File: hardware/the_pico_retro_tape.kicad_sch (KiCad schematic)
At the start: 13 parts, among them J1 SD Card Modul, J2 Conn_01x06, J3 TFT Display ST7735, Q1 BC547, SW1 UP BUTTON, SW2 DOWN BUTTON, SW3 ENTER BUTTON, SW4 PLAY BUTTON, U1 Pico

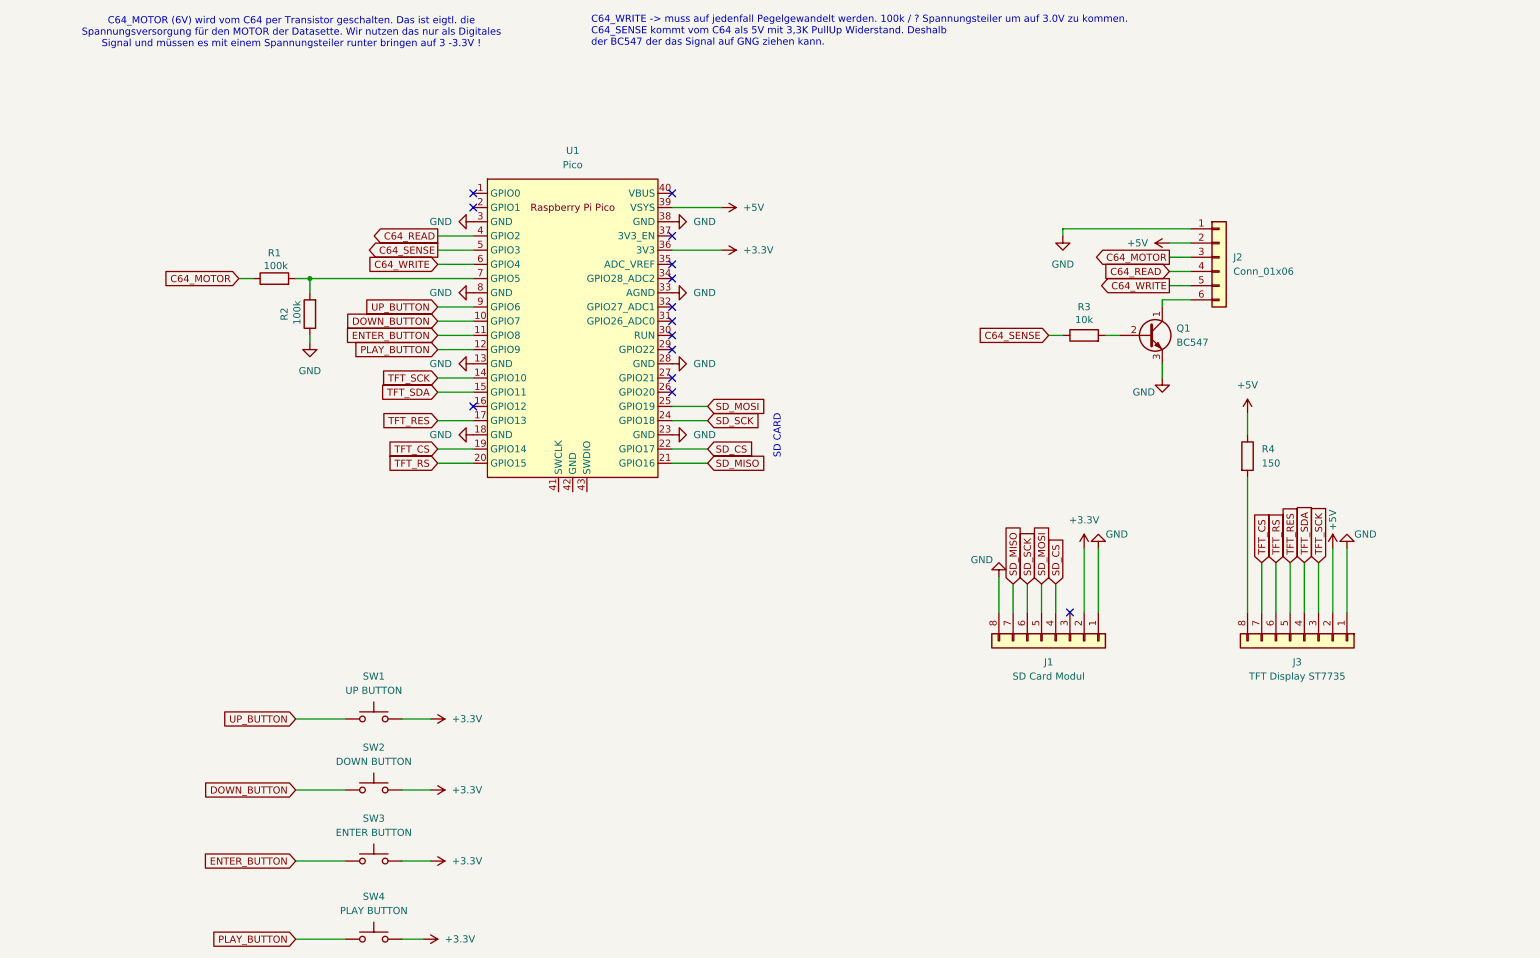
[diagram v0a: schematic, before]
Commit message: hardware:  added an optional speaker
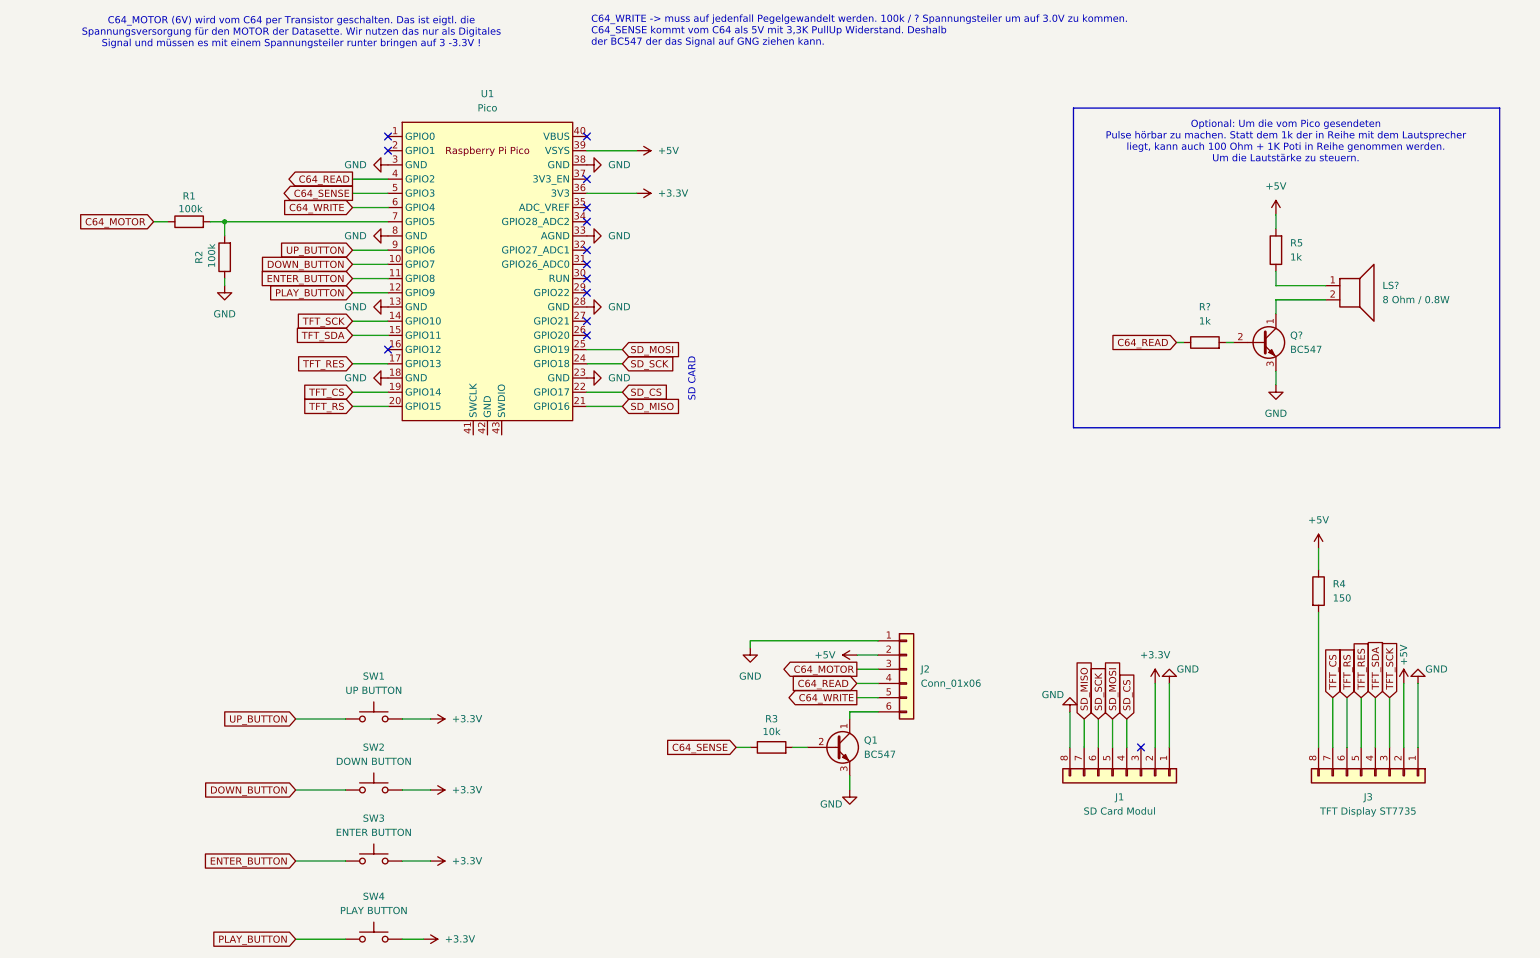
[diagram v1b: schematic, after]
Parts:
- added LS?: 8 Ohm / 0.8W, symbol Device:Speaker
- added Q?: BC547, Package_TO_SOT_THT:TO-92_Inline, symbol Transistor_BJT:BC547
- added R5, R?: 1k, symbol Device:R
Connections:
- net +5V: now also R5.2
- net C64_READ: now also R?.1
- net GND: now also Q?.3 (E)
- new net: LS?.1, R5.1
- new net: LS?.2, Q?.1 (C)
- new net: Q?.2 (B), R?.2
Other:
- note added: "Optional: Um die vom Pico gesendeten Pulse hörbar zu machen. Statt dem 1k der in Reihe mit dem Lautsprecher liegt, kann auch 100 Ohm + 1K Poti in Reihe genommen werden. Um die Lautstärke zu steuern."
- moved on the sheet: J1, J2, J3, Q1, R1, R2, R3, R4, U1

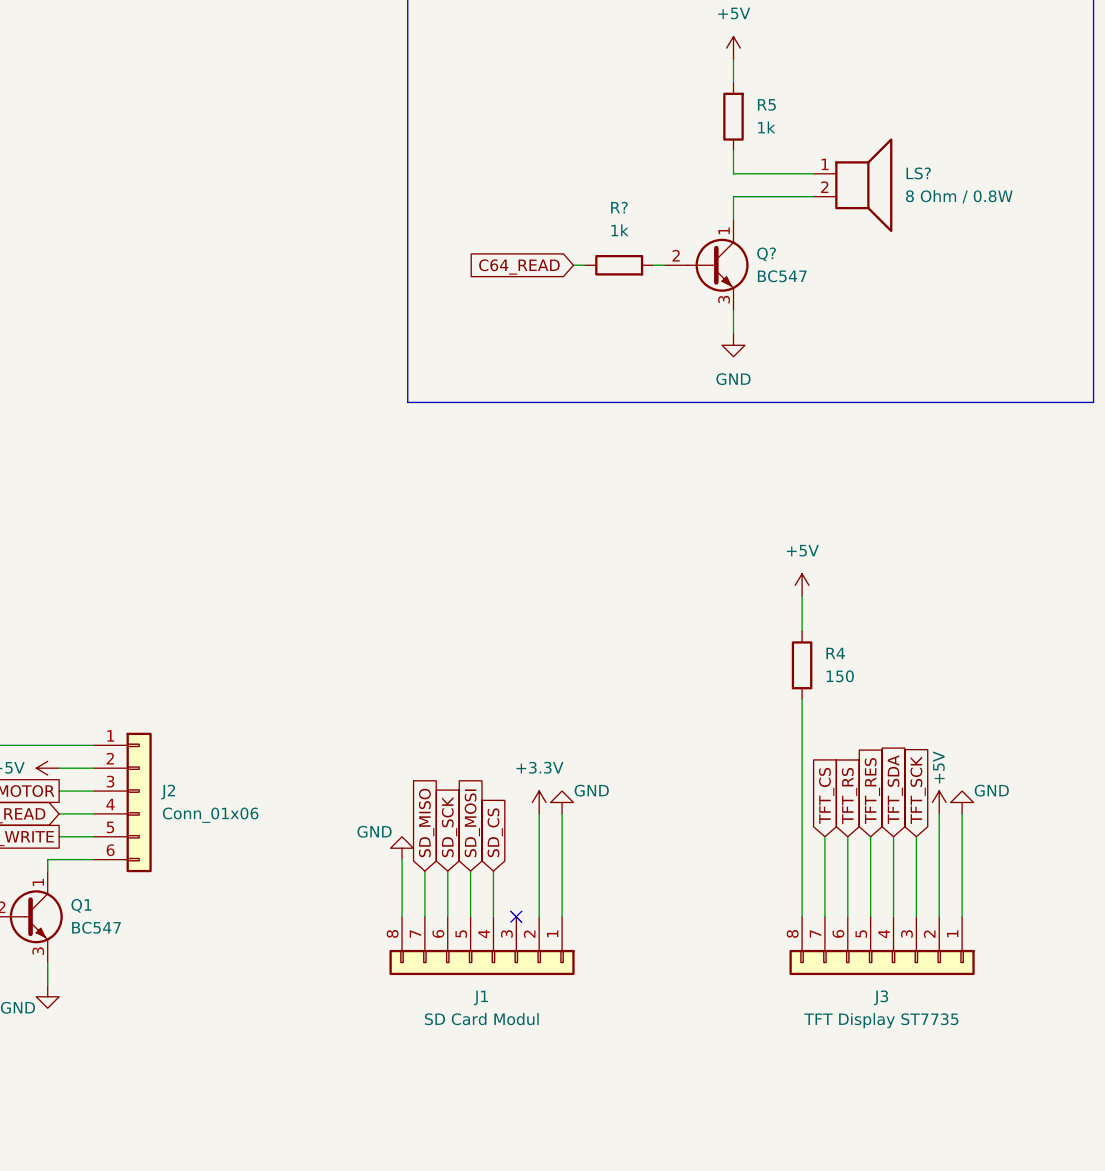
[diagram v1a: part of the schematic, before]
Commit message: Update schematic references and correct plot directory path
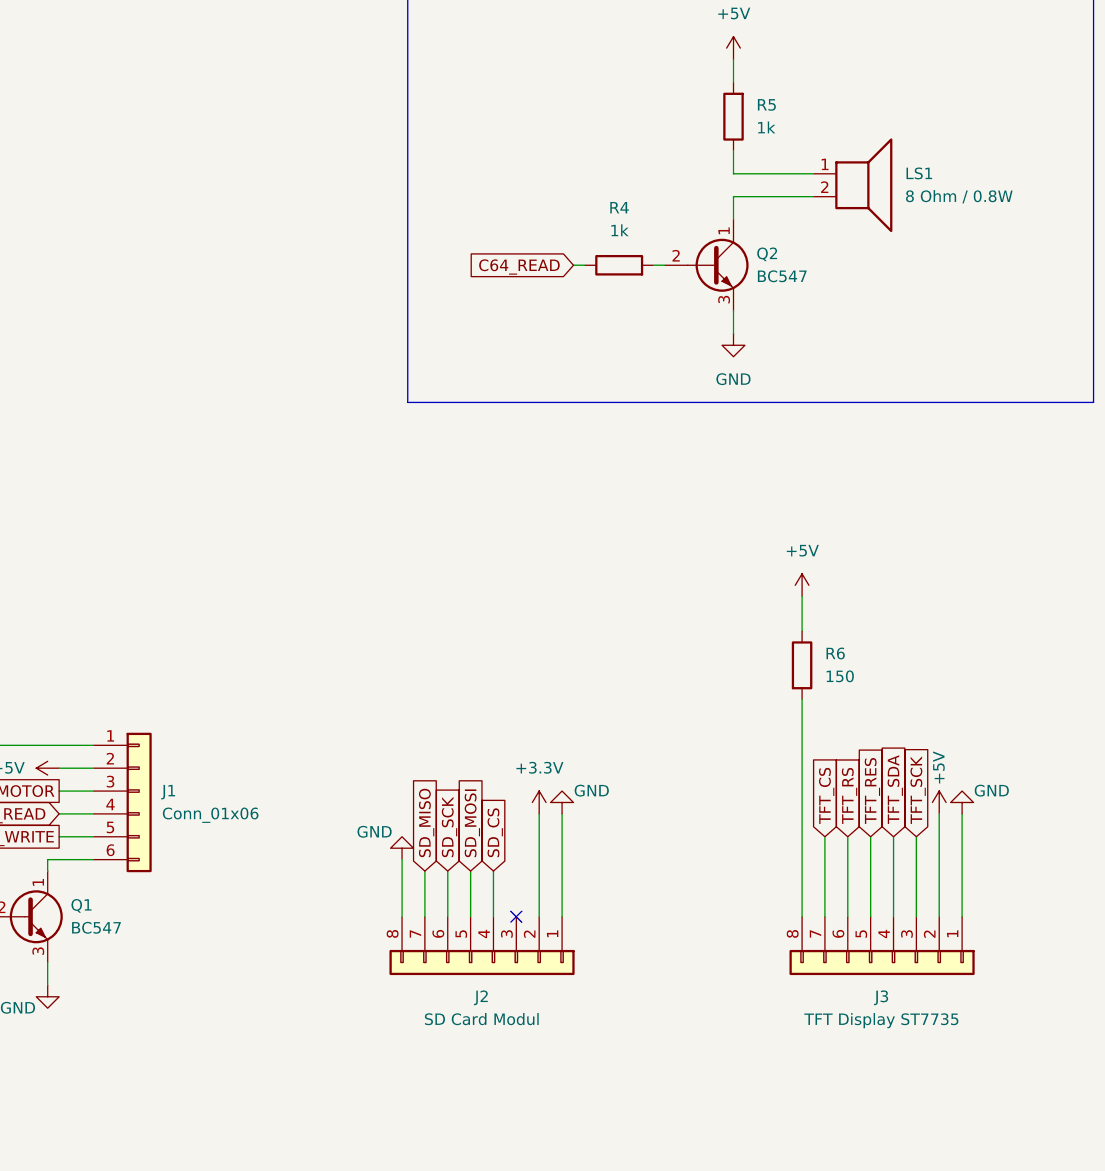
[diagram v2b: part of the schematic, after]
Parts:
- gave numbers to parts that had none: 3
- renumbered J2 to J1, J1 to J2, R4 to R6
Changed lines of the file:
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@@
 		(dnp no)
 		(fields_autoplaced yes)
-		(property "Reference" "#PWR03"
+		(property "Reference" "#PWR07"
 			(at 77.47 142.24 0)
 			(effects
@@
 			(project "the_pico_retro_tape"
 				(path "/58eb91ea-7f3f-48ec-bf75-2e4d8bc1bbc2"
-					(reference "#PWR03")
+					(reference "#PWR07")
 					(unit 1)
 				)
@@
 		(dnp no)
 		(fields_autoplaced yes)
-		(property "Reference" "#PWR04"
+		(property "Reference" "#PWR08"
 			(at 77.47 154.94 0)
 			(effects
@@
 			(project "the_pico_retro_tape"
 				(path "/58eb91ea-7f3f-48ec-bf75-2e4d8bc1bbc2"
-					(reference "#PWR04")
+					(reference "#PWR08")
 					(unit 1)
 				)
@@
 		(dnp no)
 		(fields_autoplaced yes)
-		(property "Reference" "#PWR018"
+		(property "Reference" "#PWR020"
 			(at 210.82 139.7 0)
 			(effects
@@
 			(project "the_pico_retro_tape"
 				(path "/58eb91ea-7f3f-48ec-bf75-2e4d8bc1bbc2"
-					(reference "#PWR018")
+					(reference "#PWR020")
 					(unit 1)
 				)
@@
 		(dnp no)
 		(fields_autoplaced yes)
-		(property "Reference" "#PWR021"
+		(property "Reference" "#PWR018"
 			(at 161.29 130.81 0)
 			(effects
@@
 			(project "the_pico_retro_tape"
 				(path "/58eb91ea-7f3f-48ec-bf75-2e4d8bc1bbc2"
-					(reference "#PWR021")
+					(reference "#PWR018")
 					(unit 1)
 				)
@@
 		(dnp no)
 		(fields_autoplaced yes)
-		(property "Reference" "#PWR09"
+		(property "Reference" "#PWR05"
 			(at 67.31 81.28 0)
 			(effects
@@
 			(project "the_pico_retro_tape"
 				(path "/58eb91ea-7f3f-48ec-bf75-2e4d8bc1bbc2"
-					(reference "#PWR09")
+					(reference "#PWR05")
 					(unit 1)
 				)
@@
 		(dnp no)
 		(fields_autoplaced yes)
-		(property "Reference" "#PWR06"
+		(property "Reference" "#PWR02"
 			(at 67.31 43.18 0)
 			(effects
@@
 			(project "the_pico_retro_tape"
 				(path "/58eb91ea-7f3f-48ec-bf75-2e4d8bc1bbc2"
-					(reference "#PWR06")
+					(reference "#PWR02")
 					(unit 1)
 				)
@@
 		(dnp no)
 		(fields_autoplaced yes)
-		(property "Reference" "#PWR07"
+		(property "Reference" "#PWR03"
 			(at 67.31 55.88 0)
 			(effects
@@
 			(project "the_pico_retro_tape"
 				(path "/58eb91ea-7f3f-48ec-bf75-2e4d8bc1bbc2"
-					(reference "#PWR07")
+					(reference "#PWR03")
 					(unit 1)
 				)
@@
 		(on_board yes)
 		(dnp no)
-		(property "Reference" "#PWR023"
+		(property "Reference" "#PWR025"
 			(at 255.27 139.7 0)
 			(effects
@@
 			(project "the_pico_retro_tape"
 				(path "/58eb91ea-7f3f-48ec-bf75-2e4d8bc1bbc2"
-					(reference "#PWR023")
+					(reference "#PWR025")
 					(unit 1)
 				)
@@
 		(dnp no)
 		(fields_autoplaced yes)
-		(property "Reference" "#PWR02"
+		(property "Reference" "#PWR06"
 			(at 76.2 181.61 0)
 			(effects
@@
 			(project "the_pico_retro_tape"
 				(path "/58eb91ea-7f3f-48ec-bf75-2e4d8bc1bbc2"
-					(reference "#PWR02")
+					(reference "#PWR06")
 					(unit 1)
 				)
@@
 		(dnp no)
 		(fields_autoplaced yes)
-		(property "Reference" "LS?"
+		(property "Reference" "LS1"
 			(at 251.46 64.7699 0)
 			(effects
@@
 			(project ""
 				(path "/58eb91ea-7f3f-48ec-bf75-2e4d8bc1bbc2"
-					(reference "LS?")
+					(reference "LS1")
 					(unit 1)
 				)
@@
 		(dnp no)
 		(fields_autoplaced yes)
-		(property "Reference" "Q?"
+		(property "Reference" "Q2"
 			(at 234.95 73.6599 0)
 			(effects
@@
 			(project ""
 				(path "/58eb91ea-7f3f-48ec-bf75-2e4d8bc1bbc2"
-					(reference "Q?")
+					(reference "Q2")
 					(unit 1)
 				)
@@
 		(dnp no)
 		(fields_autoplaced yes)
-		(property "Reference" "#PWR026"
+		(property "Reference" "#PWR023"
 			(at 232.41 88.9 0)
 			(effects
@@
 			(project "the_pico_retro_tape"
 				(path "/58eb91ea-7f3f-48ec-bf75-2e4d8bc1bbc2"
-					(reference "#PWR026")
+					(reference "#PWR023")
 					(unit 1)
 				)
@@
 		(dnp no)
 		(fields_autoplaced yes)
-		(property "Reference" "R4"
+		(property "Reference" "R6"
 			(at 242.57 118.1099 0)
 			(effects
@@
 			(project ""
 				(path "/58eb91ea-7f3f-48ec-bf75-2e4d8bc1bbc2"
-					(reference "R4")
+					(reference "R6")
 					(unit 1)
 				)
@@
 		(dnp no)
 		(fields_autoplaced yes)
-		(property "Reference" "#PWR05"
+		(property "Reference" "#PWR09"
 			(at 77.47 167.64 0)
 			(effects
@@
 			(project "the_pico_retro_tape"
 				(path "/58eb91ea-7f3f-48ec-bf75-2e4d8bc1bbc2"
-					(reference "#PWR05")
+					(reference "#PWR09")
 					(unit 1)
 				)
@@
 		(dnp no)
 		(fields_autoplaced yes)
-		(property "Reference" "J2"
+		(property "Reference" "J1"
 			(at 168.91 133.3499 0)
 			(effects
@@
 			(project ""
 				(path "/58eb91ea-7f3f-48ec-bf75-2e4d8bc1bbc2"
-					(reference "J2")
+					(reference "J1")
 					(unit 1)
 				)
@@
 		(dnp no)
 		(fields_autoplaced yes)
-		(property "Reference" "#PWR017"
+		(property "Reference" "#PWR016"
 			(at 138.43 135.89 0)
 			(effects
@@
 			(project ""
 				(path "/58eb91ea-7f3f-48ec-bf75-2e4d8bc1bbc2"
-					(reference "#PWR017")
+					(reference "#PWR016")
 					(unit 1)
 				)
@@
 		(on_board yes)
 		(dnp no)
-		(property "Reference" "#PWR020"
+		(property "Reference" "#PWR017"
 			(at 156.21 161.29 0)
 			(effects
@@
 			(project "the_pico_retro_tape"
 				(path "/58eb91ea-7f3f-48ec-bf75-2e4d8bc1bbc2"
-					(reference "#PWR020")
+					(reference "#PWR017")
 					(unit 1)
 				)
@@
 		(dnp no)
 		(fields_autoplaced yes)
-		(property "Reference" "J1"
+		(property "Reference" "J2"
 			(at 204.47 156.21 90)
 			(effects
@@
 			(project ""
 				(path "/58eb91ea-7f3f-48ec-bf75-2e4d8bc1bbc2"
-					(reference "J1")
+					(reference "J2")
 					(unit 1)
 				)
@@
 		(dnp no)
 		(fields_autoplaced yes)
-		(property "Reference" "#PWR025"
+		(property "Reference" "#PWR022"
 			(at 232.41 55.88 0)
 			(effects
@@
 			(project "the_pico_retro_tape"
 				(path "/58eb91ea-7f3f-48ec-bf75-2e4d8bc1bbc2"
-					(reference "#PWR025")
+					(reference "#PWR022")
 					(unit 1)
 				)
@@
 		(on_board yes)
 		(dnp no)
-		(property "Reference" "#PWR019"
+		(property "Reference" "#PWR021"
 			(at 213.36 129.54 0)
 			(effects
@@
 			(project "the_pico_retro_tape"
 				(path "/58eb91ea-7f3f-48ec-bf75-2e4d8bc1bbc2"
-					(reference "#PWR019")
+					(reference "#PWR021")
 					(unit 1)
 				)
@@
 		(on_board yes)
 		(dnp no)
-		(property "Reference" "#PWR024"
+		(property "Reference" "#PWR026"
 			(at 257.81 129.54 0)
 			(effects
@@
 			(project "the_pico_retro_tape"
 				(path "/58eb91ea-7f3f-48ec-bf75-2e4d8bc1bbc2"
-					(reference "#PWR024")
+					(reference "#PWR026")
 					(unit 1)
 				)
@@
 		(on_board yes)
 		(dnp no)
-		(property "Reference" "#PWR016"
+		(property "Reference" "#PWR019"
 			(at 195.58 134.62 0)
 			(effects
@@
 			(project "the_pico_retro_tape"
 				(path "/58eb91ea-7f3f-48ec-bf75-2e4d8bc1bbc2"
-					(reference "#PWR016")
+					(reference "#PWR019")
 					(unit 1)
 				)
@@
 		(dnp no)
 		(fields_autoplaced yes)
-		(property "Reference" "#PWR08"
+		(property "Reference" "#PWR04"
 			(at 67.31 68.58 0)
 			(effects
@@
 			(project "the_pico_retro_tape"
 				(path "/58eb91ea-7f3f-48ec-bf75-2e4d8bc1bbc2"
-					(reference "#PWR08")
+					(reference "#PWR04")
 					(unit 1)
 				)
@@
 		(dnp no)
 		(fields_autoplaced yes)
-		(property "Reference" "#PWR022"
+		(property "Reference" "#PWR024"
 			(at 240.03 115.57 0)
 			(effects
@@
 			(project "the_pico_retro_tape"
 				(path "/58eb91ea-7f3f-48ec-bf75-2e4d8bc1bbc2"
-					(reference "#PWR022")
+					(reference "#PWR024")
 					(unit 1)
 				)
@@
 		(dnp no)
 		(fields_autoplaced yes)
-		(property "Reference" "R?"
+		(property "Reference" "R4"
 			(at 219.71 68.58 90)
 			(effects
@@
 			(project ""
 				(path "/58eb91ea-7f3f-48ec-bf75-2e4d8bc1bbc2"
-					(reference "R?")
-					(unit 1)
-				)
+					(reference "R4")
+					(unit 1)
+				)
